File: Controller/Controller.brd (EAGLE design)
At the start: 100 x 80 mm, 0 parts

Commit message: Modified controller.
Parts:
- added FRAME1: FRAME-LETTER, SparkFun-Aesthetics:CREATIVE_COMMONS
- added U1: TPD4S009DBVR, Texas Instruments_By_element14_Batch_1:SOT95P280X145-6N
- added U2: TPS2511DGN, TI-TPS2511DGN:SOP65P490X110-9N
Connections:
- new net IN: U2.3
- new net VCC: U1.5
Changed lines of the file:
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@@
 <layer number="48" name="Document" color="7" fill="1" visible="yes" active="yes"/>
 <layer number="49" name="Reference" color="7" fill="1" visible="yes" active="yes"/>
+<layer number="50" name="dxf" color="7" fill="1" visible="no" active="no"/>
 <layer number="51" name="tDocu" color="7" fill="1" visible="yes" active="yes"/>
 <layer number="52" name="bDocu" color="7" fill="1" visible="yes" active="yes"/>
+<layer number="53" name="tGND_GNDA" color="7" fill="9" visible="no" active="no"/>
+<layer number="54" name="bGND_GNDA" color="1" fill="9" visible="no" active="no"/>
+<layer number="56" name="wert" color="7" fill="1" visible="no" active="no"/>
 <layer number="90" name="Modules" color="5" fill="1" visible="no" active="no"/>
 <layer number="91" name="Nets" color="2" fill="1" visible="no" active="no"/>
@@
 <layer number="97" name="Info" color="7" fill="1" visible="no" active="no"/>
 <layer number="98" name="Guide" color="6" fill="1" visible="no" active="no"/>
+<layer number="100" name="Muster" color="7" fill="1" visible="no" active="no"/>
+<layer number="101" name="Patch_Top" color="12" fill="4" visible="yes" active="yes"/>
+<layer number="102" name="Vscore" color="7" fill="1" visible="yes" active="yes"/>
+<layer number="103" name="tMap" color="7" fill="1" visible="yes" active="yes"/>
+<layer number="104" name="Name" color="16" fill="1" visible="yes" active="yes"/>
+<layer number="105" name="tPlate" color="7" fill="1" visible="yes" active="yes"/>
+<layer number="106" name="bPlate" color="7" fill="1" visible="yes" active="yes"/>
+<layer number="107" name="Crop" color="7" fill="1" visible="yes" active="yes"/>
+<layer number="108" name="tplace-old" color="10" fill="1" visible="no" active="yes"/>
+<layer number="109" name="ref-old" color="11" fill="1" visible="no" active="yes"/>
+<layer number="116" name="Patch_BOT" color="9" fill="4" visible="yes" active="yes"/>
+<layer number="121" name="_tsilk" color="7" fill="1" visible="yes" active="yes"/>
+<layer number="122" name="_bsilk" color="7" fill="1" visible="yes" active="yes"/>
+<layer number="125" name="_tNames" color="7" fill="1" visible="yes" active="yes"/>
+<layer number="144" name="Drill_legend" color="7" fill="1" visible="yes" active="yes"/>
+<layer number="151" name="HeatSink" color="7" fill="1" visible="yes" active="yes"/>
+<layer number="199" name="Contour" color="7" fill="1" visible="yes" active="yes"/>
+<layer number="200" name="200bmp" color="1" fill="10" visible="yes" active="yes"/>
+<layer number="201" name="201bmp" color="2" fill="10" visible="yes" active="yes"/>
+<layer number="202" name="202bmp" color="3" fill="10" visible="yes" active="yes"/>
+<layer number="203" name="203bmp" color="4" fill="10" visible="yes" active="yes"/>
+<layer number="204" name="204bmp" color="5" fill="10" visible="yes" active="yes"/>
+<layer number="205" name="205bmp" color="6" fill="10" visible="yes" active="yes"/>
+<layer number="206" name="206bmp" color="7" fill="10" visible="yes" active="yes"/>
+<layer number="207" name="207bmp" color="8" fill="10" visible="yes" active="yes"/>
+<layer number="208" name="208bmp" color="9" fill="10" visible="yes" active="yes"/>
+<layer number="209" name="209bmp" color="7" fill="1" visible="yes" active="yes"/>
+<layer number="210" name="210bmp" color="7" fill="1" visible="yes" active="yes"/>
+<layer number="211" name="211bmp" color="7" fill="1" visible="yes" active="yes"/>
+<layer number="212" name="212bmp" color="7" fill="1" visible="yes" active="yes"/>
+<layer number="213" name="213bmp" color="7" fill="1" visible="yes" active="yes"/>
+<layer number="214" name="214bmp" color="7" fill="1" visible="yes" active="yes"/>
+<layer number="215" name="215bmp" color="7" fill="1" visible="yes" active="yes"/>
+<layer number="216" name="216bmp" color="7" fill="1" visible="yes" active="yes"/>
+<layer number="217" name="217bmp" color="18" fill="1" visible="no" active="no"/>
+<layer number="218" name="218bmp" color="19" fill="1" visible="no" active="no"/>
+<layer number="219" name="219bmp" color="20" fill="1" visible="no" active="no"/>
+<layer number="220" name="220bmp" color="21" fill="1" visible="no" active="no"/>
+<layer number="221" name="221bmp" color="22" fill="1" visible="no" active="no"/>
+<layer number="222" name="222bmp" color="23" fill="1" visible="no" active="no"/>
+<layer number="223" name="223bmp" color="24" fill="1" visible="no" active="no"/>
+<layer number="224" name="224bmp" color="25" fill="1" visible="no" active="no"/>
+<layer number="250" name="Descript" color="3" fill="1" visible="no" active="no"/>
+<layer number="251" name="SMDround" color="12" fill="11" visible="no" active="no"/>
+<layer number="254" name="cooling" color="7" fill="1" visible="yes" active="yes"/>
 </layers>
 <board>
@@
 </autorouter>
 <elements>
+<element name="FRAME1" library="SparkFun-Aesthetics" package="CREATIVE_COMMONS" value="FRAME-LETTER" x="21.59" y="-7.62"/>
+<element name="U1" library="Texas Instruments_By_element14_Batch_1" package="SOT95P280X145-6N" value="TPD4S009DBVR" x="5.08" y="-13.97">
+<attribute name="PACKAGE" value="SOT-23-6" x="5.08" y="-13.97" size="1.778" layer="27" display="off"/>
+<attribute name="OC_NEWARK" value="33R2191" x="5.08" y="-13.97" size="1.778" layer="27" display="off"/>
+<attribute name="MPN" value="TPD4S009DBVR" x="5.08" y="-13.97" size="1.778" layer="27" display="off"/>
+<attribute name="SUPPLIER" value="TEXAS INSTRUMENTS" x="5.08" y="-13.97" size="1.778" layer="27" display="off"/>
+<attribute name="OC_FARNELL" value="1855143" x="5.08" y="-13.97" size="1.778" layer="27" display="off"/>
+</element>
+<element name="U2" library="TI-TPS2511DGN" package="SOP65P490X110-9N" value="TPS2511DGN" x="7.62" y="-25.4">
+<attribute name="PACKAGE" value="MSOP-8" x="7.62" y="-25.4" size="1.778" layer="27" display="off"/>
+<attribute name="OC_NEWARK" value="44W8612" x="7.62" y="-25.4" size="1.778" layer="27" display="off"/>
+<attribute name="MPN" value="TPS2511DGN " x="7.62" y="-25.4" size="1.778" layer="27" display="off"/>
+<attribute name="SUPPLIER" value="TEXAS INSTRUMENTS " x="7.62" y="-25.4" size="1.778" layer="27" display="off"/>
+<attribute name="OC_FARNELL" value="2211372 " x="7.62" y="-25.4" size="1.778" layer="27" display="off"/>
+</element>
 </elements>
 <signals>
+<signal name="VCC">
+<contactref element="U1" pad="5"/>
+</signal>
+<signal name="IN">
+<contactref element="U2" pad="3"/>
+</signal>
 </signals>
 </board>

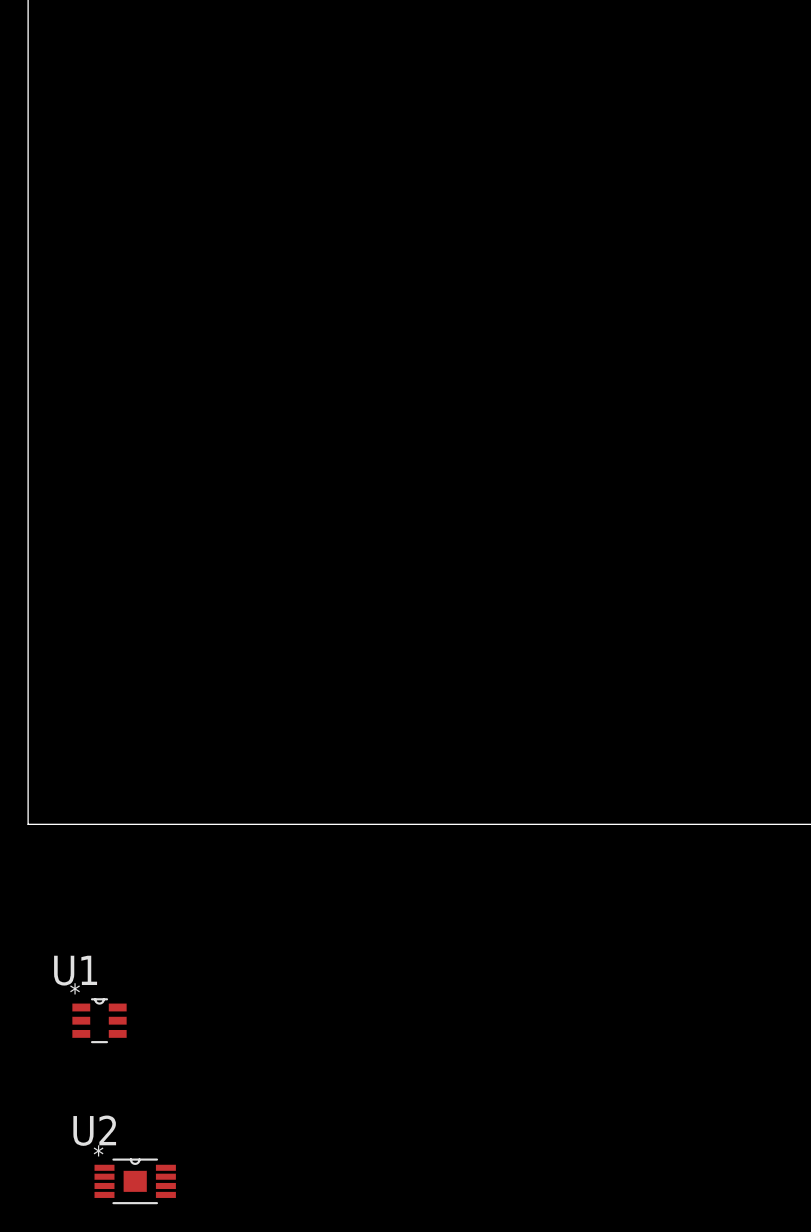
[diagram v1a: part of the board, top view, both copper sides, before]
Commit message: Modified ESD/Controller board and schematic.
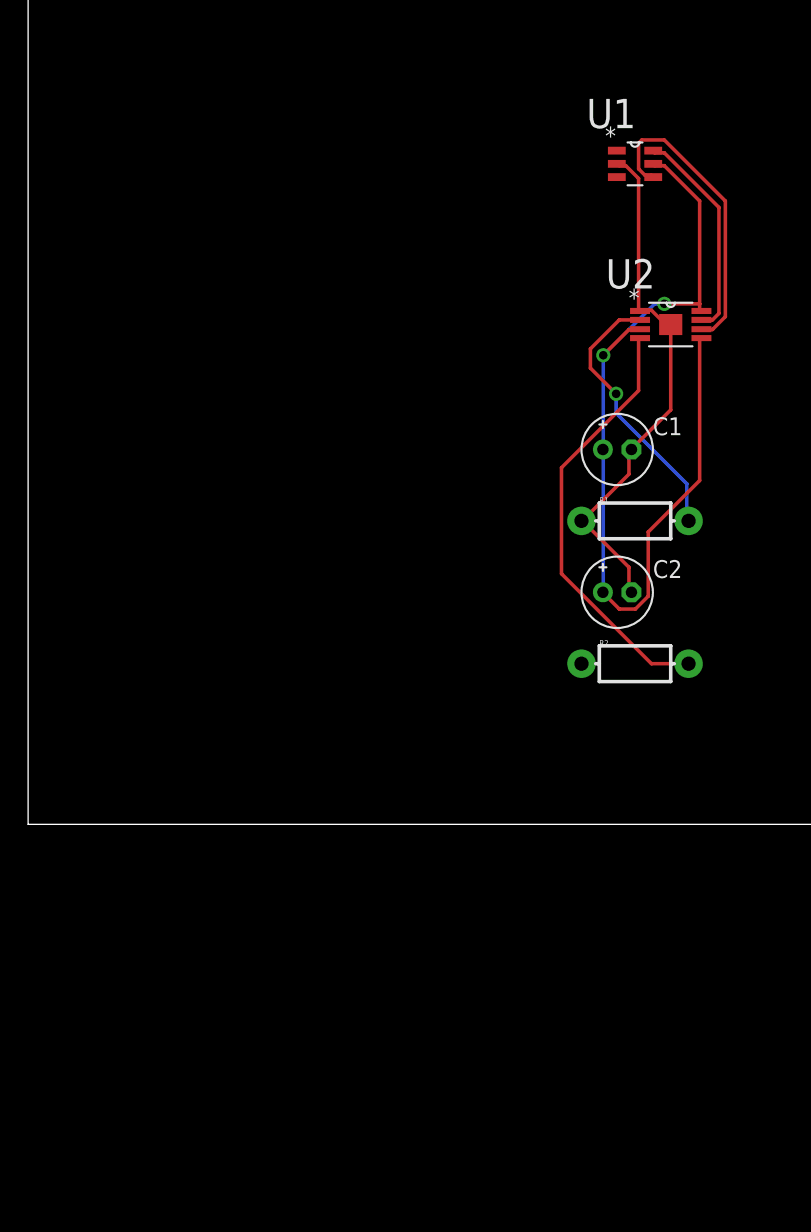
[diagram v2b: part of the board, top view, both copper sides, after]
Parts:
- added C1, C2: (no value), adafruit:E2-5
- added R1, R2: (no value), SparkFun-Passives:AXIAL-0.3-KIT
- moved U1 71.9 mm to (43.2, 47.0)
- moved U2 71.9 mm to (45.7, 35.6)
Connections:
- removed net IN: U2.3
- removed net VCC: U1.5
- new net N$1: U1.3
- new net N$2: U1.1
- new net N$3: C1.+, C2.+, U1.5, U2.3, U2.5, U2.8
- new net N$4: C1.-, C2.-, R1.P$1, U1.2, U2.1, U2.9
- new net N$5: U1.6, U2.7
- new net N$6: U1.4, U2.6
- new net N$7: R1.P$2, U2.2
- new net N$8: R2.P$2, U2.4
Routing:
- net N$3: track 0.00 -> 65.0 mm, vias 0 -> 2
- net N$4: track 0.00 -> 37.3 mm
- net N$8: track 0.00 -> 30.8 mm
- net N$6: track 0.00 -> 21.5 mm
- net N$7: track 0.00 -> 19.5 mm, vias 0 -> 1
- net N$5: track 0.00 -> 15.3 mm

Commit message: Modified controller
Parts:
- added JP2: (no value), adafruit:1X03-CLEANBIG
- added U$1: SPARKFUN_USB_A, sparkfun-usb-a:USB_4UCON_18666_318
- moved R2 46.2 mm to (3.81, 35.6), turned to 90 degrees
- moved U2 41.3 mm to (5.08, 27.9)
- moved R1 38.2 mm to (7.62, 35.6), turned to 270 degrees
- moved C2 37.2 mm to (5.08, 21.6)
- moved U1 35.9 mm to (12.7, 27.9), turned to 180 degrees
- moved C1 29.6 mm to (12.7, 21.6)
- moved FRAME1 11.5 mm to (33.0, -8.89)
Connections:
- new net N$9: JP2.2, R2.P$1
- net N$1: now also U$1.USB+
- net N$2: now also U$1.USB-
- net N$3: now also JP2.1, U$1.USB_5V
- net N$4: now also JP2.3, U$1.USB_GND
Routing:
- net N$1: track 0.00 -> 20.8 mm, vias 0 -> 1
- net N$6: track 21.5 -> 4.65 mm
- net N$8: track 30.8 -> 15.7 mm, vias 0 -> 1
- net N$2: track 0.00 -> 14.3 mm, vias 0 -> 1
- net N$4: track 37.3 -> 49.8 mm
- net N$7: track 19.5 -> 8.74 mm, vias 1 -> 0
- net N$9: track 0.00 -> 10.5 mm
- net N$3: track 65.0 -> 56.9 mm, vias 2 -> 0
- net N$5: track 15.3 -> 9.05 mm
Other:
- board size 100 x 80 mm -> 18.7 x 43.2 mm
